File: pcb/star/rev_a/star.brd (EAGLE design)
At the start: 46.2 x 40 mm, 42 parts, among them J2 TC2030-JLINK-NL, J3 MICRO_USB_B_HIROSE_ZX62-B-5PA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, J4 TC2030-JLINK-NL, U2 LTC4065, U3 TRIPOINT, U4 TPS715AXX, U5 NRF51822QF, X1 EPSON-FA-128

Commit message: tag coming along
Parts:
- D1: value (none) -> GREEN
- D2: value (none) -> BLUE
- moved R6 3.55 mm to (-12.0, 0.27), turned to 195 degrees
- moved C14 2.01 mm to (1.87, -3.63), turned to 240 degrees
- moved R1 1.94 mm to (2.44, -2.21), turned to 240 degrees
- moved R2 1.76 mm to (3.41, -1.65), turned to 240 degrees
- moved R10 1.13 mm to (6.29, 1.68), turned to 120 degrees
- moved J4 1.11 mm to (17.8, 0.50), turned to 150 degrees
- moved C18 1.02 mm to (7.68, 1.17)
- moved U2 0.80 mm to (8.80, 2.90)
- moved C17 0.60 mm to (4.26, 5.50), turned to 120 degrees
- moved L1 0.59 mm to (-0.51, -5.74)
- moved L3 0.56 mm to (0.53, -4.98)
- moved LOGO1 0.56 mm to (11.8, -16.9)
- moved D1 0.56 mm to (5.00, -17.1), turned to 270 degrees
- moved R12 0.56 mm to (5.02, -16.0), turned to 0 degrees
- moved A2 0.56 mm to (14.1, -7.91)
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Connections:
- new net N$1: A3.A, U3.9
- new net N$2: A2.A, U3.26
- new net N$3: A1.A, U3.43
- new net N$4: J4.2, U3.28
- new net N$7: J4.4, U3.29
- new net N$8: J4.3, U3.30
- net DW_INT: now also U3.38
- net GND: now also U3.10, U3.18, U3.25, U3.27, U3.42, U3.44, U3.8
- net I2C_SCL: now also U3.37
- net I2C_SDA: now also U3.36
- net N$6: now also U5.25; no longer U5.43
- net VCC: now also U3.17
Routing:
- net VCC: track 18.3 -> 76.2 mm, vias 2 -> 7
- net VBAT: track 7.30 -> 43.9 mm
- net GND: track 128.1 -> 93.3 mm, vias 27 -> 35
- net I2C_SCL: track 0.00 -> 20.9 mm, vias 0 -> 1
- net I2C_SDA: track 0.00 -> 20.8 mm, vias 0 -> 1
- net N$5: track 7.15 -> 27.1 mm, vias 2 -> 3
- net DW_INT: track 0.00 -> 15.5 mm, vias 0 -> 1
- net SWDCLK: track 0.00 -> 14.7 mm, vias 0 -> 1
- net N$8: track 0.00 -> 12.8 mm
- net SWDIO/!RESET: track 0.00 -> 12.2 mm, vias 0 -> 1
- net N$4: track 0.00 -> 10.6 mm
- net VUSB: track 16.1 -> 25.0 mm, vias 0 -> 1
- net N$6: track 5.06 -> 13.3 mm, vias 0 -> 1
- net N$7: track 0.00 -> 8.03 mm
- net N$1: track 0.00 -> 3.58 mm
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- added copper zone on layer 1, net GND
- added copper zone on layer 16, net GND

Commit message: board is basically there
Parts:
- moved LOGO1 30.9 mm to (3.98, 13.0)
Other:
- board text added: "A"
- board text added: "STM"
- board text added: "TITLE"
- board text added: "nRF"

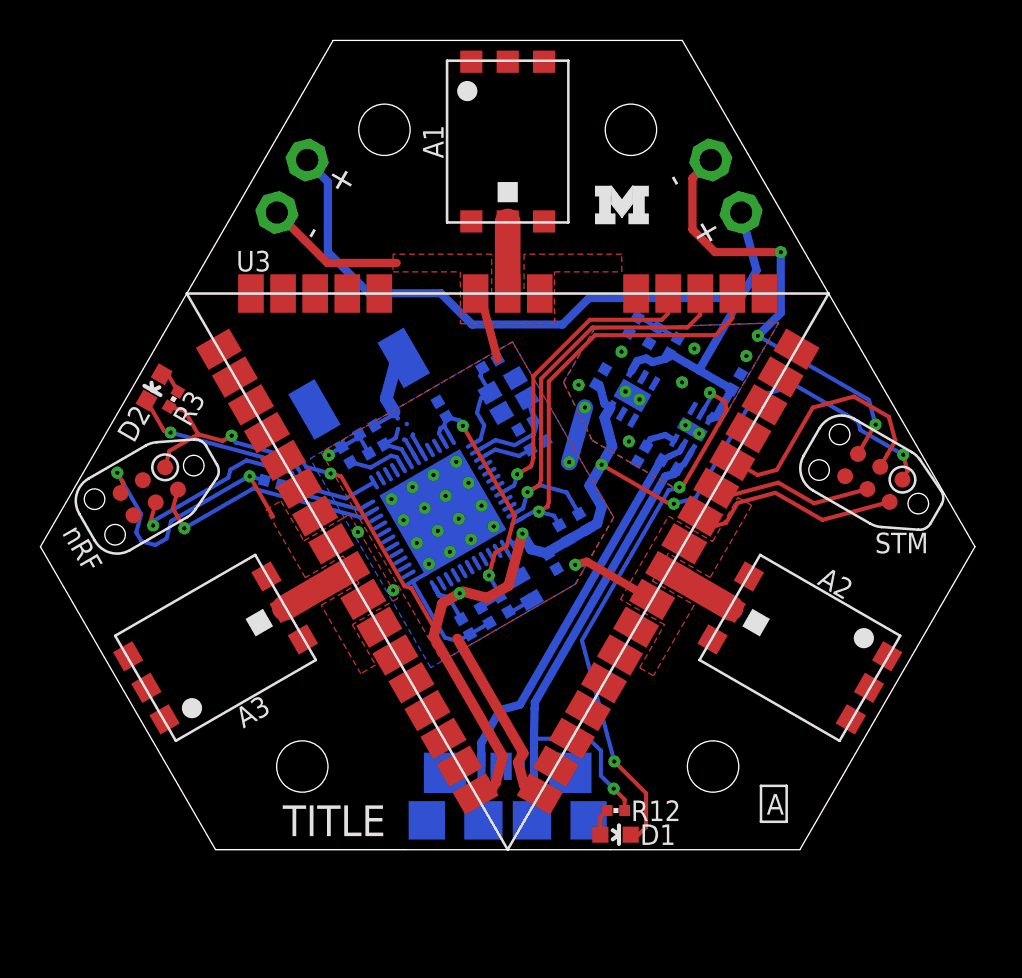
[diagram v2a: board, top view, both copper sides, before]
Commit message: renamed parts, added bom
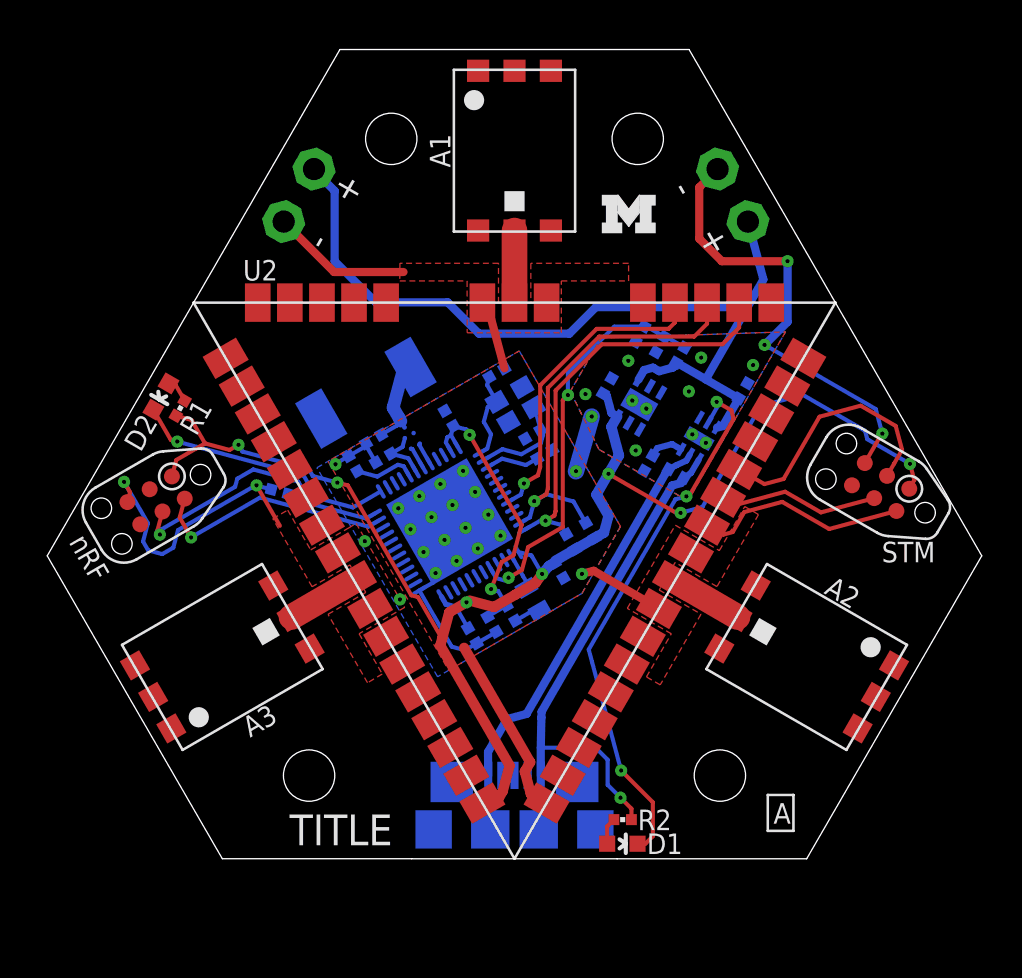
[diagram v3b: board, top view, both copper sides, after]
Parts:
- removed C15: 0.1uF, passives:0402_CAP
- removed C17: 0.47uF, passives:0402_CAP
- removed C18: 1uF, passives:0402_CAP
- removed L3: 10uH, passives:0603_CAP
- removed R10: 2k 1%, passives:0402_RES
- removed R12: 1k, passives:0402_RES
- removed R14: 2.2M, passives:0402_RES
- removed R15: 10M, passives:0402_RES
- removed U$3, U$4: BAT_HOLE, connector:BATTERY_HOLE
- removed U5: NRF51822QF, chips:QFN-48-6MM
- added C12: 1uF, passives:0402_CAP
- added C5: 2.2nF, passives:0402_CAP
- added C9: 0.1uF, passives:0402_CAP
- added J1: TC2030-JLINK-NL, connector:TC2030-IDC-NL
- added J5: BAT_HOLE, connector:BATTERY_HOLE
- added L2: 10uH, passives:0603_CAP
- added R4, R5: 10k, passives:0402_RES
- added R7: 2.2M, passives:0402_RES
- added R8: 10M, passives:0402_RES
- added U1: NRF51822QF, chips:QFN-48-6MM
- C10: value 47nF -> 0.1uF
- C11: value 0.1uF -> 0.47uF
- C4: value 0.1uF -> 1nF
- C6: value 1nF -> 47nF
- C7: value 100nF -> 0.1uF
- C8: value 2.2nF -> 0.1uF
- J4: value TC2030-JLINK-NL -> BAT_HOLE; device connector:TC2030-IDC-NL -> connector:BATTERY_HOLE
- R1, R2: value 10k -> 1k
- R3: value 1k -> 2k 1%
- U2: value LTC4065 -> TRIPOINT; device chips:DFN-6/2MM -> tripoint:TRIPOINT
- U3: value TRIPOINT -> LTC4065; device tripoint:TRIPOINT -> chips:DFN-6/2MM
- moved J2 36.2 mm to (18.1, 0.05), turned to 150 degrees
- moved R3 23.7 mm to (6.63, 1.23), flipped to the bottom, turned to 120 degrees
- moved R1 19.9 mm to (-16.5, 3.95), flipped to the top
- moved C10 19.9 mm to (11.3, 4.81), turned to 120 degrees
- moved J4 15.6 mm to (10.8, 14.5), turned to 120 degrees
- moved R2 14.9 mm to (5.35, -16.4), flipped to the top, turned to 0 degrees
- moved C4 14.3 mm to (-3.24, 3.44), turned to 60 degrees
- moved C11 13.8 mm to (4.59, 5.05), turned to 120 degrees
- moved C13 11.8 mm to (8.01, 0.72), turned to 30 degrees
- moved C8 10.4 mm to (-2.08, -7.30), turned to 240 degrees
- moved U3 9.68 mm to (9.13, 2.45), flipped to the bottom, turned to 210 degrees
- moved U2 9.26 mm to (0.00, 0.00), flipped to the top, turned to 0 degrees
- moved C6 5.17 mm to (-7.99, 1.21)
- moved X1 0.56 mm to (0.04, 4.13)
- moved LOGO1 0.56 mm to (4.32, 12.6)
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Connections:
- net !CHRG: now also R2.1; no longer R12.1
- net !CHRG1: now also R1.1; no longer R3.1
- net AVDD: now also C12.1, C4.1, U1.35, U1.36; no longer C13.1, C6.1, U5.35, U5.36
- net BATIN: now also C9.2, R7.2, R8.1, U1.5; no longer C15.2, R14.2, R15.1
- net DCC: now also L2.2, U1.2; no longer L3.2, U5.2
- net DW_INT: now also U1.44, U2.38; no longer U3.38, U5.44
- net GND: now also C12.2, C5.2, C9.1, J1.5, J4.N, J5.N, R3.1, R7.1, U1.13, U1.33, U1.34, U1.GND, U2.10, U2.18, U2.25, U2.27, U2.42, U2.44, U2.8, U3.1, U3.5, U3.7; no longer C15.1, C17.2, C18.2, J4.5, R10.1, R14.1, U$3.N, U$4.N, U2.1, U2.5, U2.7, U3.10, U3.18, U3.25, U3.27, U3.42, U3.44, U3.8, U5.13, U5.33, U5.34, U5.GND
- net I2C_SCL: now also R5.1, U1.47, U2.37; no longer R2.1, U3.37, U5.47
- net I2C_SDA: now also R4.1, U1.48, U2.36; no longer R1.1, U3.36, U5.48
- net N$1: now also U2.9; no longer U3.9
- net N$10: now also U1.38; no longer U5.38
- net N$13: now also R3.2, U3.6; no longer R10.2, U2.6
- net N$15: now also C6.1, U1.29; no longer C10.1, U5.29
- net N$17: now also U1.39; no longer U5.39
- net N$18: now also U1.31; no longer U5.31
- net N$19: now also U1.32; no longer U5.32
- net N$2: now also U2.26; no longer U3.26
- net N$20: now also C5.1, U1.30; no longer C8.1, U5.30
- net N$3: now also U2.43; no longer U3.43
- net N$37: now also L2.1; no longer L3.1
- net N$4: now also J2.2, U2.28; no longer J4.2, U3.28
- net N$5: now also U3.2; no longer U2.2
- net N$6: now also U1.25; no longer U5.25
- net N$7: now also J2.4, U2.29; no longer J4.4, U3.29
- net N$8: now also J2.3, U2.30; no longer J4.3, U3.30
- net N$9: now also U1.37; no longer U5.37
- net SWDCLK: now also J1.4, U1.24; no longer J2.4, U5.24
- net SWDIO/!RESET: now also J1.2, U1.23; no longer J2.2, U5.23
- net VBAT: now also C10.1, J4.P, J5.P, R8.2, U3.3; no longer C4.1, R15.2, U$3.P, U$4.P, U2.3
- net VCC: now also C8.1, J1.1, R4.2, R5.2, U1.1, U1.12, U2.17; no longer C17.1, J4.1, R2.2, R3.2, U3.17, U5.1, U5.12
- net VUSB: now also C13.1, R2.2, U3.4; no longer C18.1, R12.2, U2.4
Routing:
- net BATIN: track 2.29 -> 19.9 mm, vias 0 -> 2
- net VCC: track 76.2 -> 75.3 mm
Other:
- board text added: "2015/07/14"
- board text added: "Brad Campbell"

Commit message: updated bom
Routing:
- net GND: track 93.3 -> 112.3 mm
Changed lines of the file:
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@@
 <polygon width="0" layer="16" thermals="no">
 <vertex x="8.58004375" y="-0.63286875"/>
-<vertex x="13.40604375" y="7.725990625"/>
+<vertex x="12.948559375" y="6.93360625" curve="121.920922"/>
+<vertex x="12.491590625" y="7.695321875"/>
 <vertex x="4.28395625" y="7.420053125"/>
 <vertex x="2.75995625" y="4.78040625"/>
@@
 <vertex x="2.75995625" y="4.78040625"/>
 <vertex x="4.28395625" y="7.420053125"/>
-<vertex x="13.40604375" y="7.725990625"/>
+<vertex x="12.491590625" y="7.695321875" curve="-121.919971"/>
+<vertex x="12.948559375" y="6.93360625"/>
 </polygon>
 <wire x1="-12.032940625" y1="-0.06880625" x2="-12.7660125" y2="0.127621875" width="0.2032" layer="16"/>
@@
 <polygon width="0" layer="16" thermals="no">
 <vertex x="-9.7741125" y="1.004446875"/>
-<vertex x="0.2345375" y="6.7829375"/>
+<vertex x="-0.20559375" y="6.528828125" curve="-90.024482"/>
+<vertex x="0.48845625" y="6.3427"/>
 <vertex x="5.24354375" y="-1.901565625"/>
 <vertex x="3.7248375" y="-4.5320375"/>
@@
 <wire x1="-12.760059375" y1="0.131059375" x2="-11.604359375" y2="-1.87066875" width="0.2032" layer="1"/>
 <polygon width="0" layer="1">
-<vertex x="0.2345375" y="6.7829375"/>
+<vertex x="5.24354375" y="-1.901565625"/>
+<vertex x="0.48845625" y="6.3427" curve="90.024964"/>
+<vertex x="-0.20559375" y="6.528828125"/>
 <vertex x="-9.2241875" y="1.321946875"/>
 <vertex x="-3.2551875" y="-9.016646875"/>
 <vertex x="3.343909375" y="-5.20665"/>
 <vertex x="3.9153375" y="-4.202084375"/>
-<vertex x="5.24354375" y="-1.901565625"/>
 </polygon>
 <via x="3.0439125" y="0.830775" extent="1-16" drill="0.2032"/>
@@
 <vertex x="5.644746875" y="11.117303125"/>
 </polygon>
-<wire x1="-11.417996875" y1="13.17895625" x2="-8.924546875" y2="10.685509375" width="0.4064" layer="1"/>
-<wire x1="-8.924546875" y1="10.685509375" x2="-5.490965625" y2="10.685503125" width="0.4064" layer="1"/>
 <wire x1="10.044971875" y1="15.77703125" x2="9.139425" y2="14.871478125" width="0.4064" layer="1"/>
 <wire x1="9.139425" y1="14.871478125" x2="9.139421875" y2="12.33650625" width="0.4064" layer="1"/>
@@
 <wire x1="-8.8524625" y1="1.175284375" x2="-8.8429375" y2="1.210846875" width="0.2032" layer="16"/>
 <wire x1="-8.8429375" y1="1.210846875" x2="-8.202290625" y2="1.580721875" width="0.2032" layer="16"/>
+<wire x1="-11.417996875" y1="13.17895625" x2="-11.417996875" y2="12.73174375" width="0.4064" layer="16"/>
+<wire x1="-11.417996875" y1="12.73174375" x2="-7.8824625" y2="9.196209375" width="0.4064" layer="16"/>
+<wire x1="-7.8824625" y1="9.196209375" x2="-4.299528125" y2="9.196209375" width="0.4064" layer="16"/>
+<wire x1="-4.299528125" y1="9.196209375" x2="-2.11371875" y2="7.0104" width="0.4064" layer="16"/>
+<wire x1="-2.11371875" y1="7.0104" x2="3.06916875" y2="7.0104" width="0.4064" layer="16"/>
+<wire x1="3.06916875" y1="7.0104" x2="4.896684375" y2="8.837915625" width="0.4064" layer="16"/>
+<wire x1="4.896684375" y1="8.837915625" x2="8.001896875" y2="8.837915625" width="0.4064" layer="16"/>
+<wire x1="8.001896875" y1="8.837915625" x2="9.2341375" y2="7.605675" width="0.4064" layer="16"/>
+<wire x1="9.2341375" y1="7.605675" x2="9.2341375" y2="6.447778125" width="0.4064" layer="16"/>
 </signal>
 <signal name="VCC">
@@
 <wire x1="-9.9388125" y1="15.7409875" x2="-8.894565625" y2="14.69674375" width="0.4064" layer="16"/>
 <wire x1="-8.894565625" y1="14.69674375" x2="-8.8945625" y2="11.21890625" width="0.4064" layer="16"/>
-<wire x1="-8.8945625" y1="11.21890625" x2="-6.862565625" y2="9.186903125" width="0.4064" layer="16"/>
-<wire x1="-6.862565625" y1="9.186903125" x2="-3.306565625" y2="9.18690625" width="0.4064" layer="16"/>
-<wire x1="-3.306565625" y1="9.18690625" x2="-1.757165625" y2="7.637503125" width="0.4064" layer="16"/>
+<wire x1="-8.8945625" y1="11.21890625" x2="-7.579153125" y2="9.90349375" width="0.4064" layer="16"/>
+<wire x1="-7.579153125" y1="9.90349375" x2="-4.023153125" y2="9.903496875" width="0.4064" layer="16"/>
+<wire x1="-4.023153125" y1="9.903496875" x2="-1.757165625" y2="7.637503125" width="0.4064" layer="16"/>
 <wire x1="-1.757165625" y1="7.637503125" x2="2.713228125" y2="7.637503125" width="0.4064" layer="16"/>
 <wire x1="2.713228125" y1="7.637503125" x2="4.025753125" y2="8.950025" width="0.4064" layer="16"/>
-<wire x1="4.025753125" y1="8.950025" x2="11.52409375" y2="8.95003125" width="0.4064" layer="16"/>
 <wire x1="9.46014375" y1="5.375171875" x2="8.017515625" y2="6.20806875" width="0.4064" layer="16"/>
 <wire x1="8.017515625" y1="6.20806875" x2="7.9844125" y2="6.1992" width="0.4064" layer="16"/>
@@
 <wire x1="-9.9388125" y1="15.7409875" x2="-9.92561875" y2="15.748603125" width="0.2032" layer="16"/>
 <wire x1="-9.92561875" y1="15.748603125" x2="-9.918" y2="15.777034375" width="0.2032" layer="16"/>
+<wire x1="4.025753125" y1="8.950025" x2="4.63023125" y2="9.554503125" width="0.4064" layer="16"/>
+<wire x1="4.63023125" y1="9.554503125" x2="10.21960625" y2="9.554503125" width="0.4064" layer="16"/>
+<wire x1="10.21960625" y1="9.554503125" x2="11.26786875" y2="8.506240625" width="0.4064" layer="16"/>
+<wire x1="11.26786875" y1="8.506240625" x2="11.52409375" y2="8.95003125" width="0" layer="19" extent="16-16"/>
 </signal>
 <signal name="BATIN">

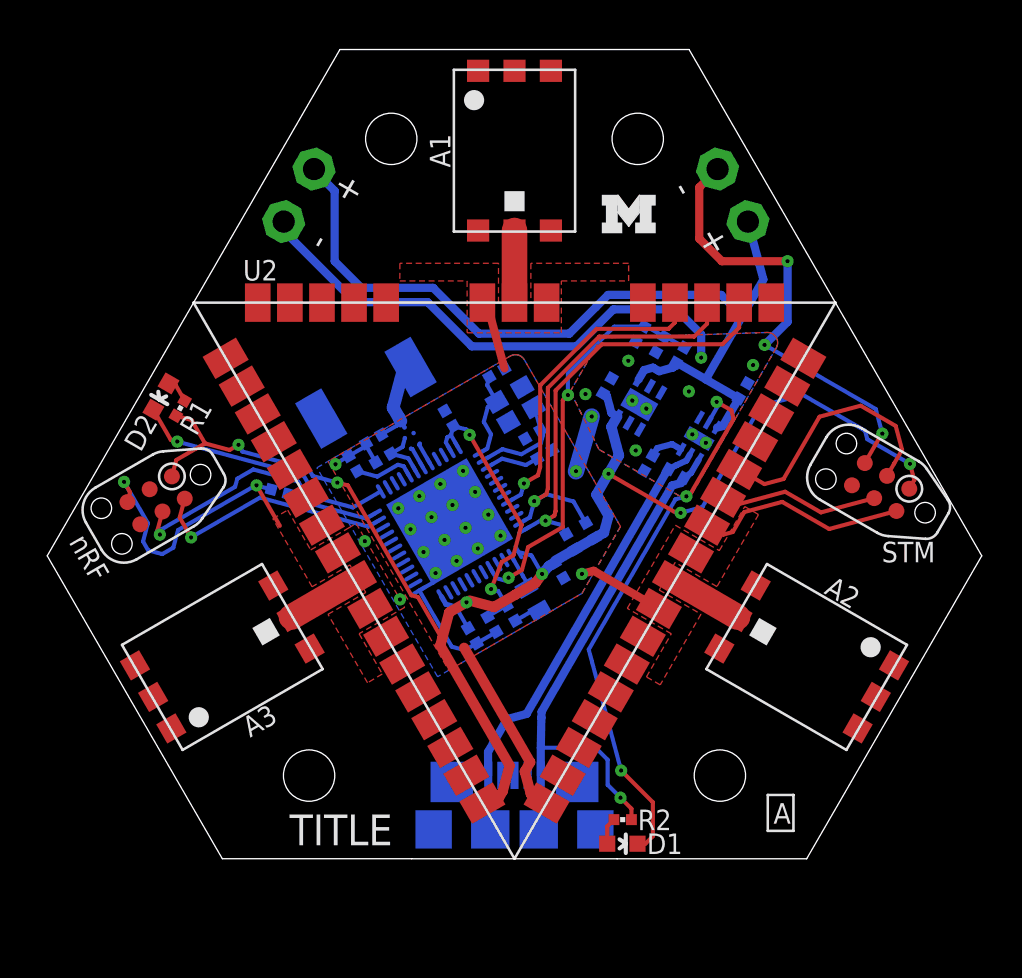
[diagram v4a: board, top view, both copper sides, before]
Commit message: added debug pads
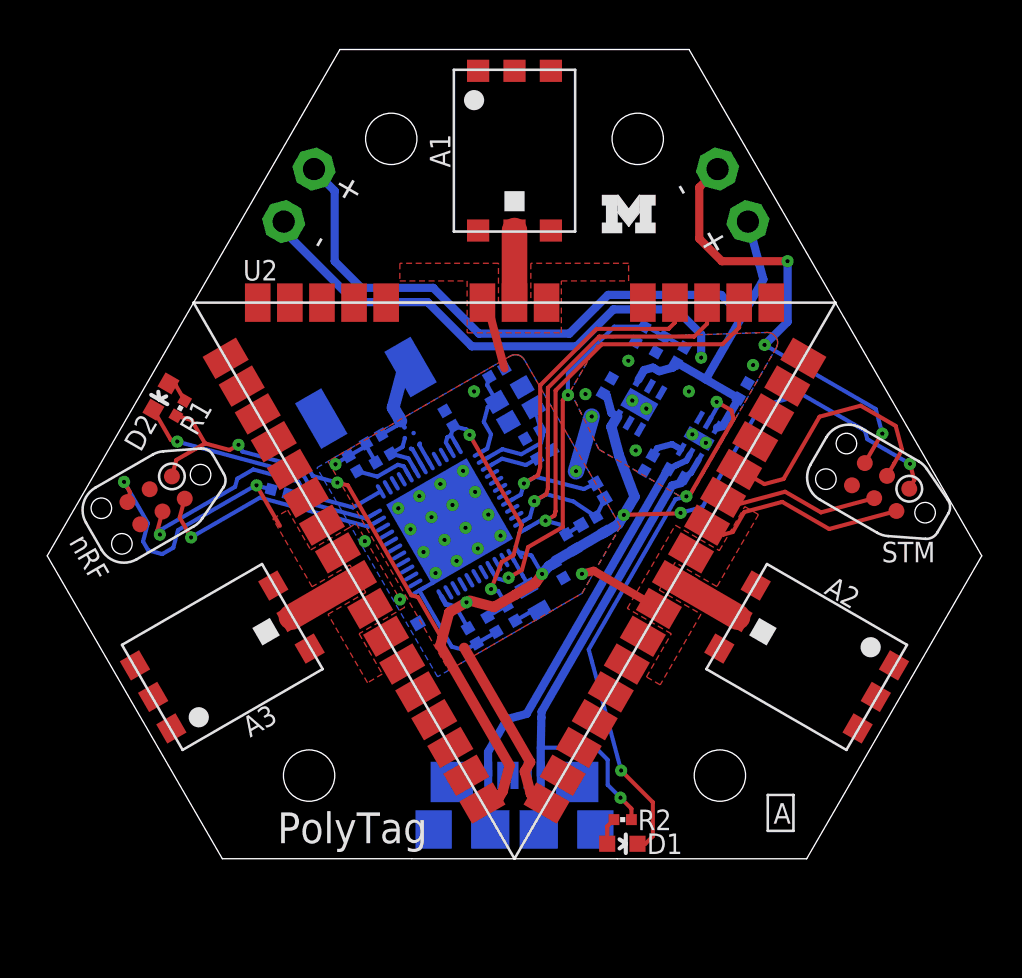
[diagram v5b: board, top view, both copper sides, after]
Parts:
- added TP1, TP2, TP3, TP4: TPTP06SQ, testpad:TP06SQ
- moved R5 0.59 mm to (4.25, -1.80)
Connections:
- net DW_INT: now also TP3.TP
- net GND: now also TP4.TP
- net I2C_SCL: now also TP1.TP
- net I2C_SDA: now also TP2.TP
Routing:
- net DW_INT: track 15.5 -> 19.3 mm
- net I2C_SCL: track 20.9 -> 22.0 mm
- net I2C_SDA: track 20.8 -> 21.7 mm
- net VCC: track 75.3 -> 74.5 mm
- net VBAT: track 44.3 -> 44.9 mm
- net GND: vias 35 -> 36
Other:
- board text added: "2015/07/15"
- board text added: "PolyTag"
- board text removed: "2015/07/14"
- board text removed: "TITLE"
